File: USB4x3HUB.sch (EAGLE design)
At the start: 93 parts, among them IC1 IC_USB_TUSB2036, IC10 IC_TTL_SINGLE_74_139_FLAT, IC2 IC_USB_FSUSB74, IC3 IC_POWER_TPS2041C, IC4 IC_POWER_TPS2041C, IC5 IC_POWER_TPS2041C, IC6 LDO4_3.3_SOT223, IC7 LDO4_5.0_SOT223, IC8 LDO4_5.0_SOT223, IC9 LDO4_5.0_SOT223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

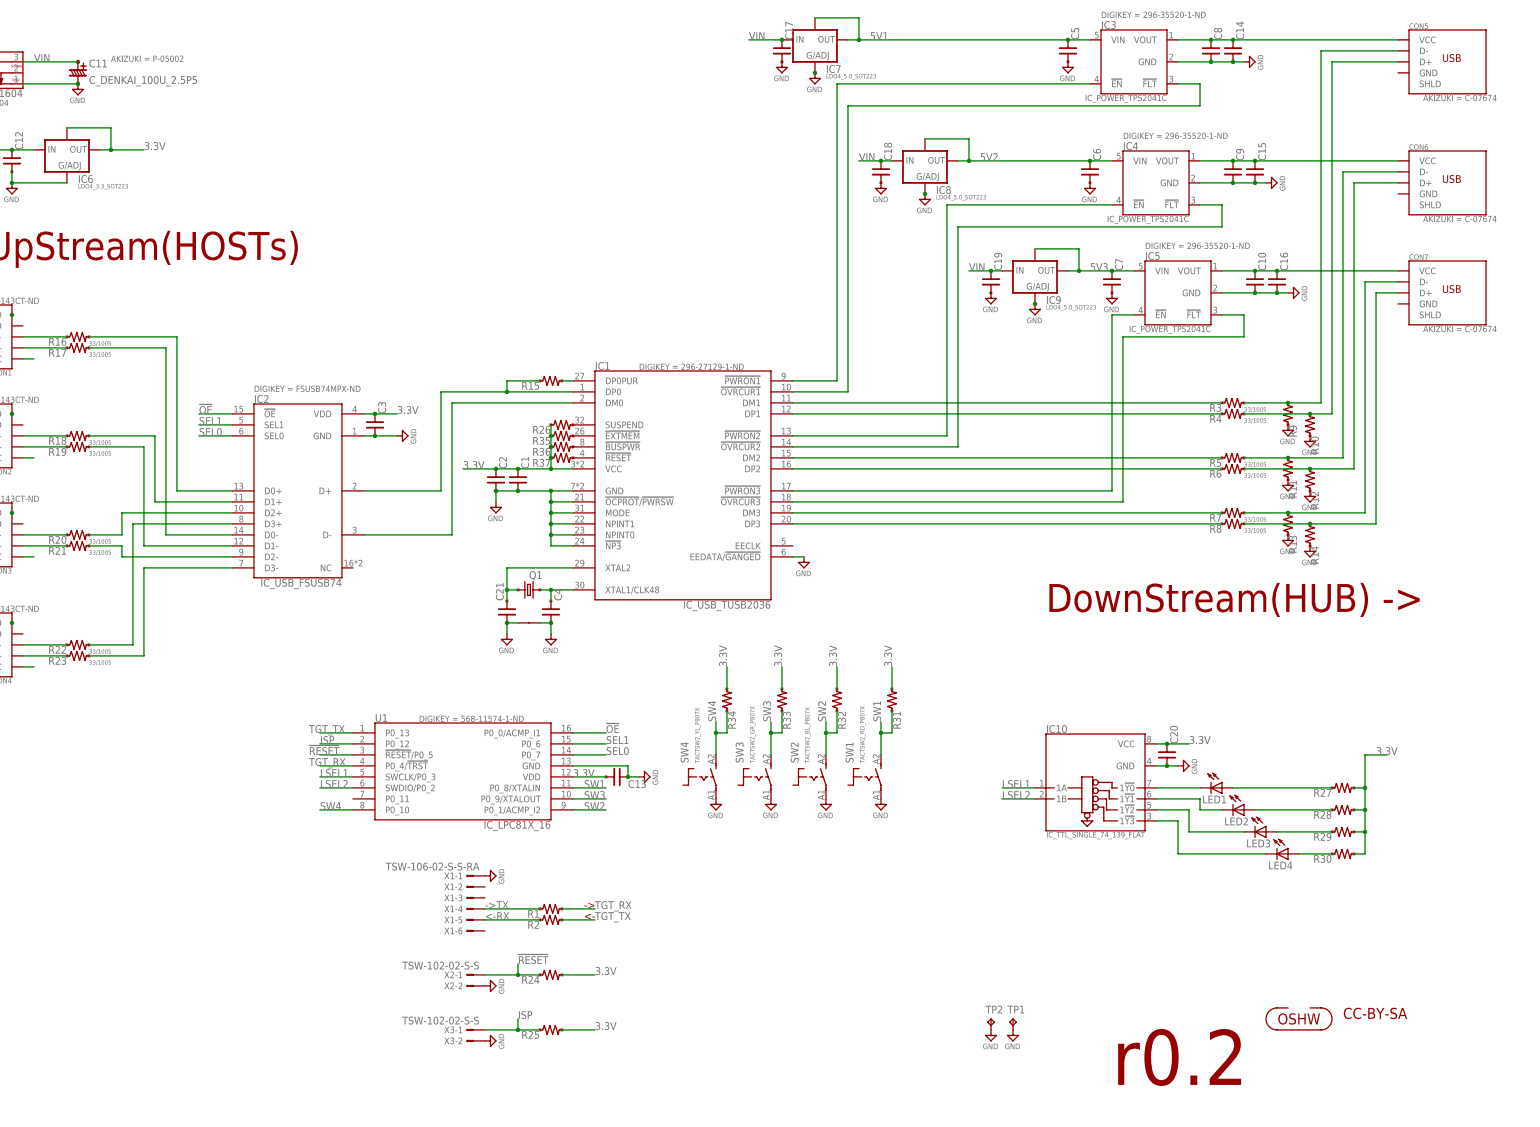
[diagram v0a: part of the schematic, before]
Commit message: [ r0.3 ] move IC1 and surroundings; replace U1 to use TSSOP(JDH16); ICON_REVISION
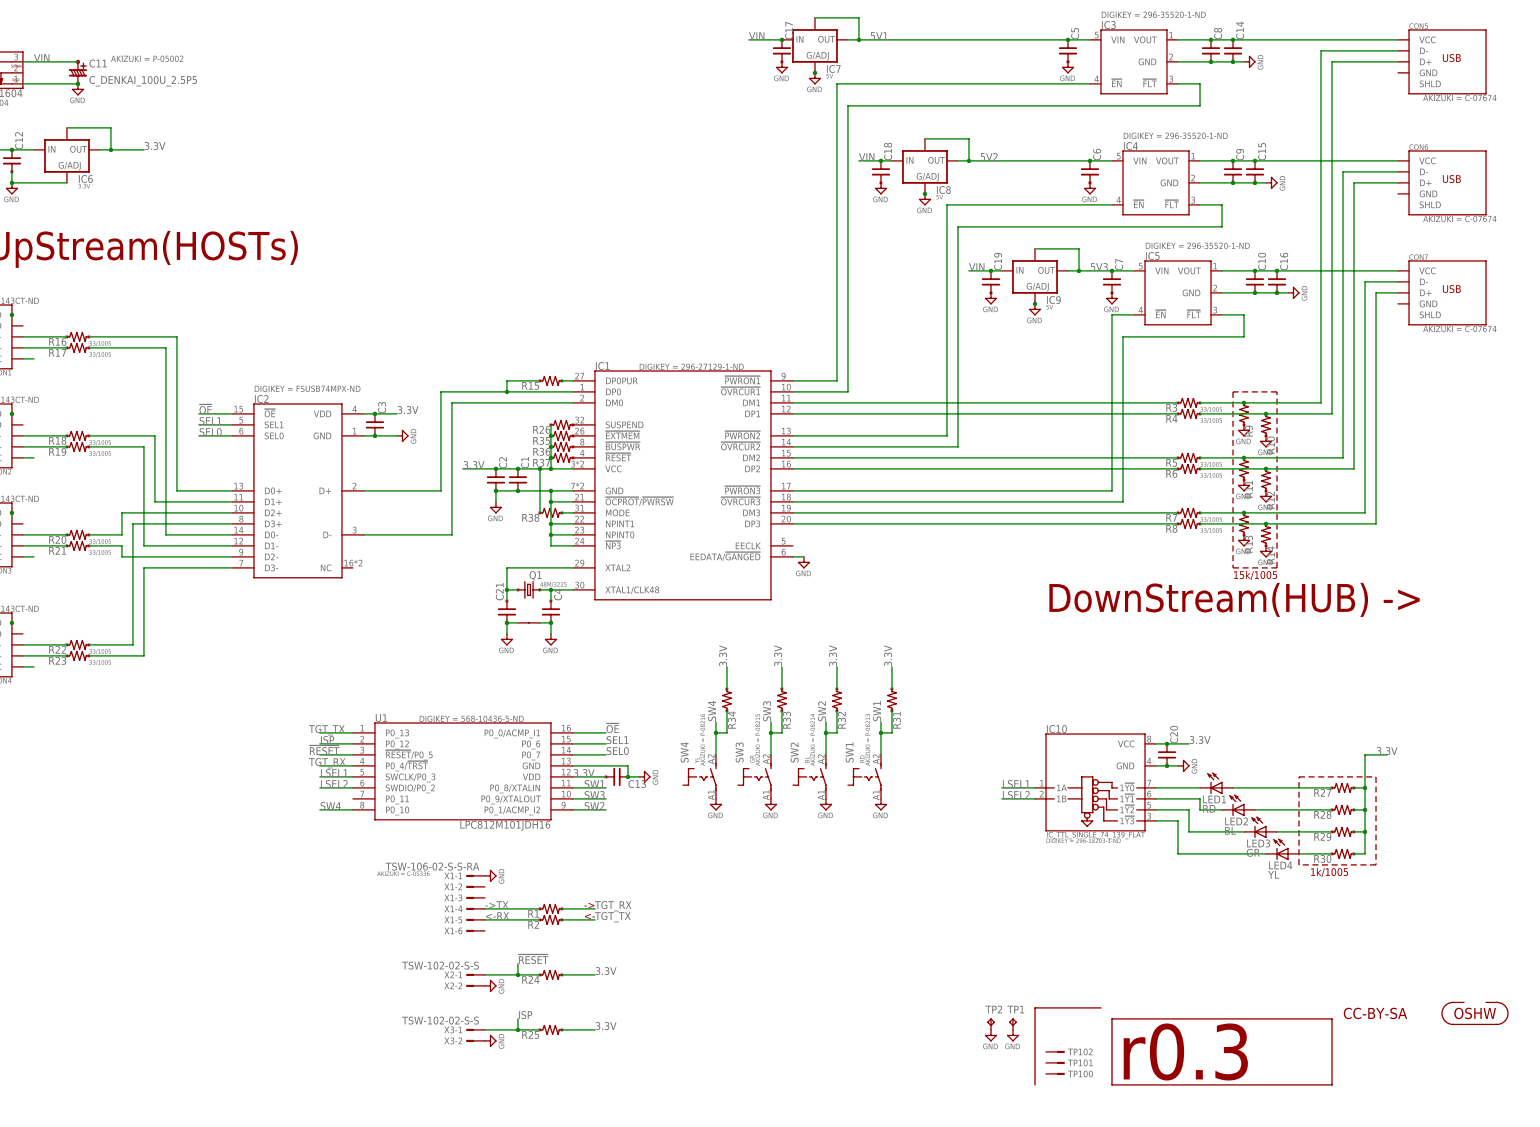
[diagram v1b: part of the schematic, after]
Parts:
- removed U$1: ICON_OSHW, mylib:ICON_OSHW
- added ICON1: OSHW, mylib:ICON_OSHW
- added ICON2: r0.3, mylib:ICON_REVISION
- added R38: (no value), mylib:R_US_10K_1005
- added TP100, TP101, TP102: (no value), mylib:TESTPAD_F
- C21, C4: device mylib:C_SMD_12P_1005 -> mylib:C_SMD_18P_1005
- IC1: value IC_USB_TUSB2036 -> (none)
- IC2: value IC_USB_FSUSB74 -> (none)
- IC3, IC4, IC5: value IC_POWER_TPS2041C -> (none)
- IC6: value LDO4_3.3_SOT223 -> 3.3V
- IC7, IC8, IC9: value LDO4_5.0_SOT223 -> 5V
- LED1: value (none) -> RD; device led_local:LEDCHIPLED_0805 -> led_local:LEDRDCHIPLED_0805
- LED2: value (none) -> BL; device led_local:LEDCHIPLED_0805 -> led_local:LEDBLCHIPLED_0805
- LED3: value (none) -> GR; device led_local:LEDCHIPLED_0805 -> led_local:LEDGRCHIPLED_0805
- LED4: value (none) -> YL; device led_local:LEDCHIPLED_0805 -> led_local:LEDYLCHIPLED_0805
- PCB1, TP1, TP2: NOT_COMPONENT (none) -> YES
- Q1: value (none) -> 48M/3225; device mylib:CRYSTAL4_6.0M_2520 -> mylib:CRYSTAL4_48M_3225
- R27, R28, R29, R30: device mylib:R_US_100R_1005 -> mylib:R_US_1.0K_1005
- SW1: value TACTSW2_RD_P807X -> RD
- SW2: value TACTSW2_BL_P807X -> BL
- SW3: value TACTSW2_GR_P807X -> GR
- SW4: value TACTSW2_YL_P807X -> YL
- U1: value IC_LPC81X_16 -> LPC812M101JDH16; device mylib:IC_LPC81X_16 -> mylib:IC_LPC81X_16_JDH16
- X1: AKIZUKI (none) -> C-05336
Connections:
- new net N$63: IC1.MODE, R38.2
- net 3.3V: now also R38.1
- net GND: no longer IC1.MODE
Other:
- note added: "15k/1005"
- note added: "1k/1005"
- note removed: "r0.2"
- moved on the sheet: R10, R11, R12, R13, R14, R3, R4, R5, R6, R7, R8, R9

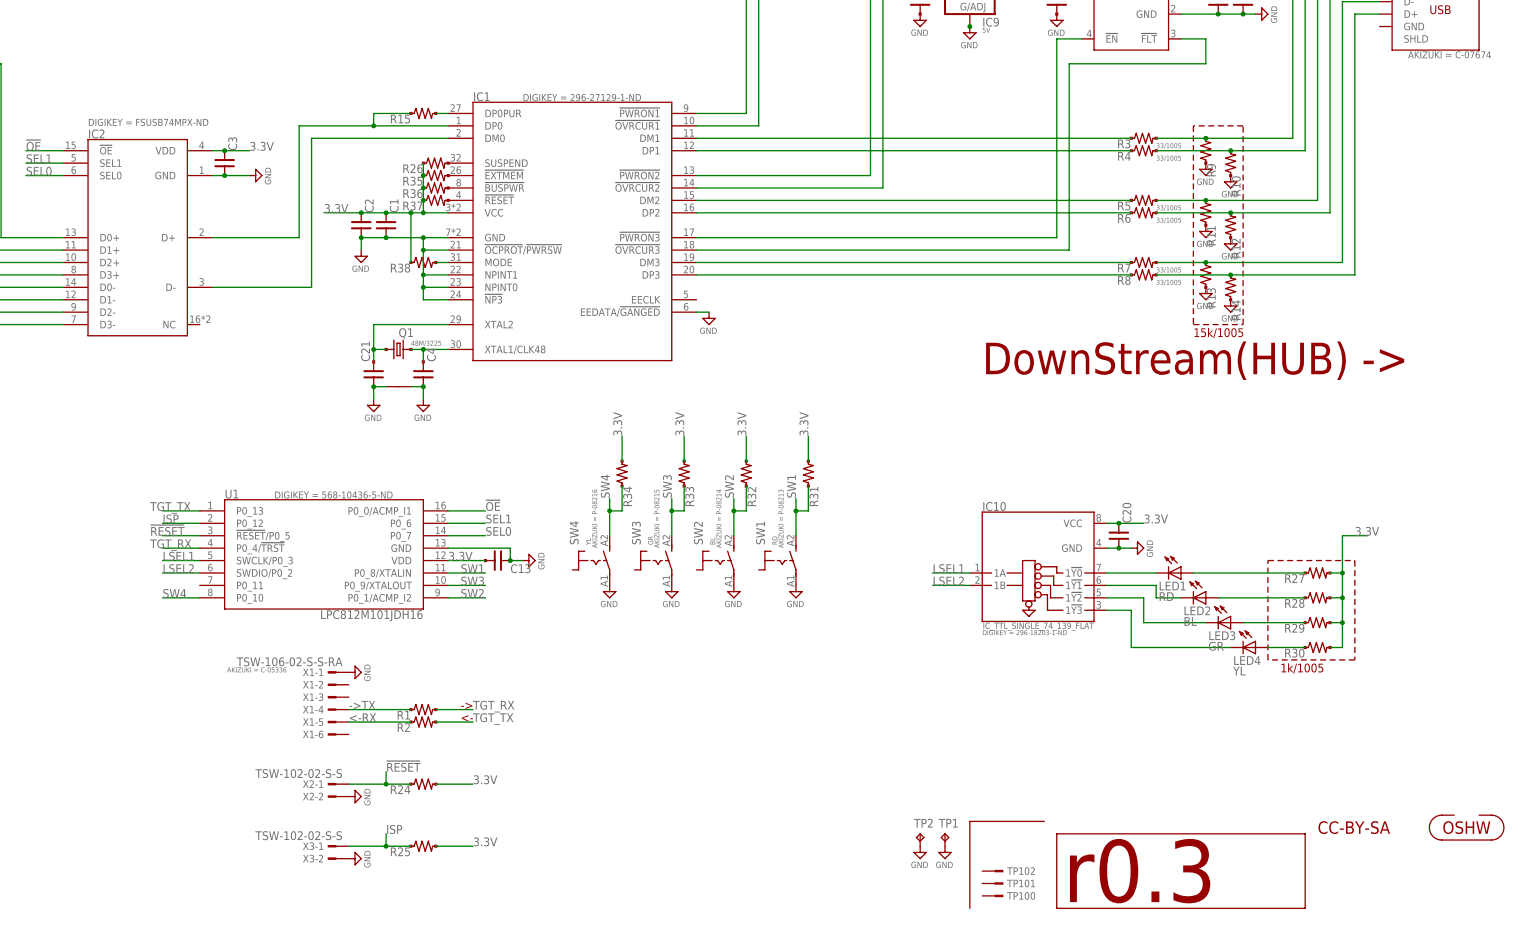
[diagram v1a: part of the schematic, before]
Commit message: [ r0.3 ] update BOM; fix HUB BUS line
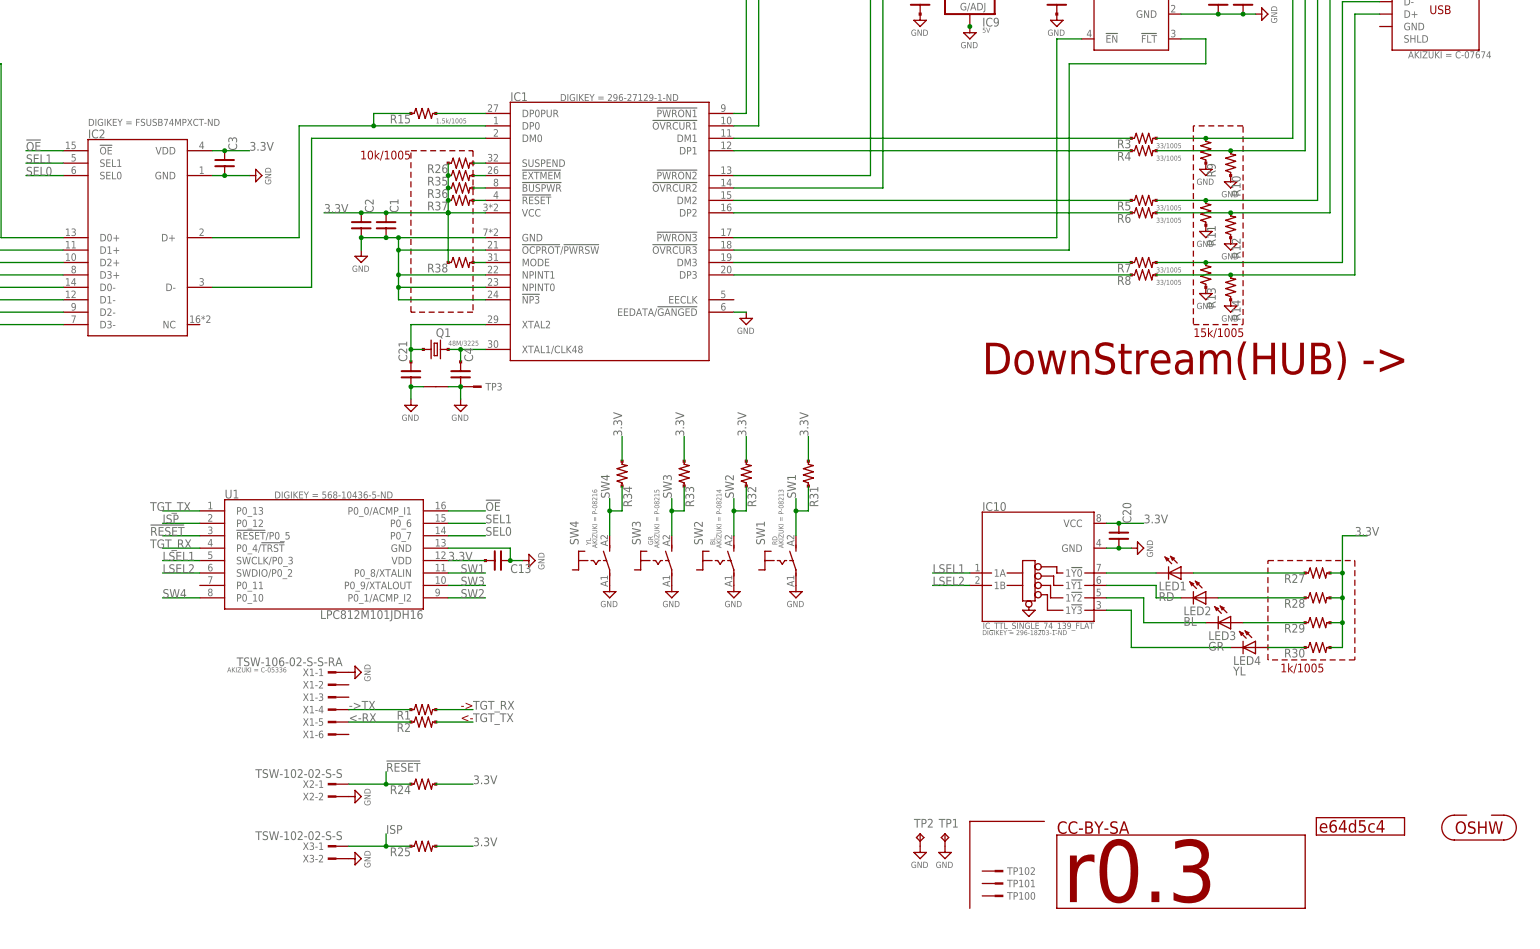
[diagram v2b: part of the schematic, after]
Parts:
- added TP3: (no value), mylib:TESTPAD
- added U$1: e64d5c4, git-revision:GIT-REVISION
- R15: value (none) -> 1.5k/1005
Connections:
- net GND: now also TP3.1
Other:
- note added: "10k/1005"
- moved on the sheet: C21, C4, IC1, Q1, R26, R35, R36, R37, R38
